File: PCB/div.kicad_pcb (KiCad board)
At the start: 2 copper layers, 31.5 x 110.5 mm, 74 parts, among them J1 Rst, J10 OUT, J2 Bus Gate Reset, J3 Clk, J4 PWR, J5 OUT, J6 OUT, J7 OUT, J8 OUT, J9 OUT, Q1 BC547, Q10 BC547, Q2 BC547, Q3 BC547, Q4 BC557, Q5 BC547, Q6 BC547, Q7 BC547, Q8 BC547, Q9 BC547, U1 4024

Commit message: :pencil2: Fix relevant DRC warnings
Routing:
- net Net-(D1-K): track 17.3 -> 16.7 mm
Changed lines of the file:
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@@
   (segment (start 143.383 50.165) (end 145.161 51.943) (width 0.2032) (layer "F.Cu") (net 4))
   (segment (start 144.1578 59.6772) (end 138.7982 59.6772) (width 0.2032) (layer "B.Cu") (net 4))
-  (segment (start 138.303 59.182) (end 138.684 58.801) (width 0.2032) (layer "B.Cu") (net 4))
   (segment (start 138.7982 59.6772) (end 138.303 59.182) (width 0.2032) (layer "B.Cu") (net 4))
   (segment (start 145.161 58.674) (end 144.1578 59.6772) (width 0.2032) (layer "B.Cu") (net 4))

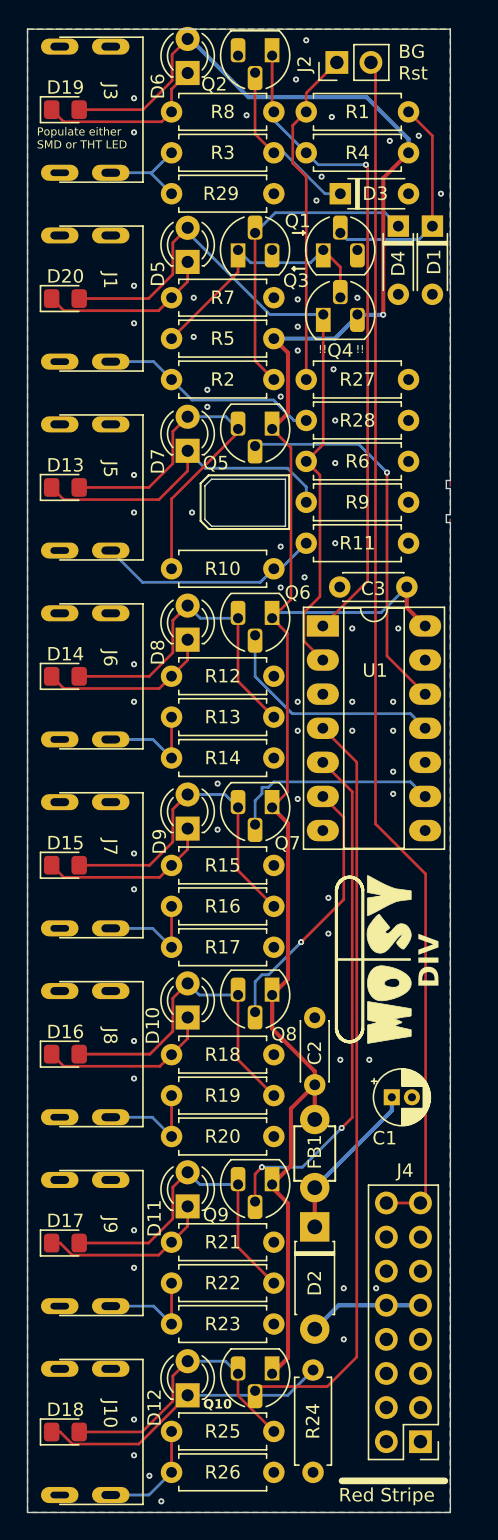
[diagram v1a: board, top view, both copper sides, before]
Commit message: :adhesive_bandaid: Fix DRC errors
Display of errors was accidentally switched off und with the change
of transistor footprints trace overlaps have been introduced.

These errors are now fixed.
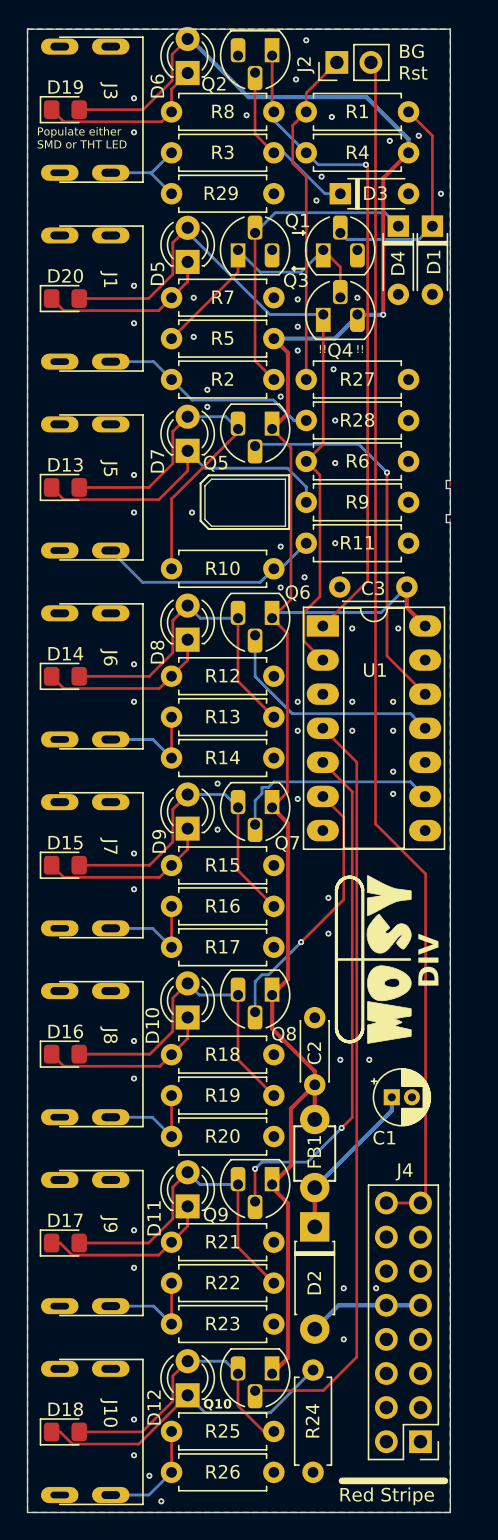
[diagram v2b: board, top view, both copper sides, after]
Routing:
- net Net-(D12-K): track 22.1 -> 23.2 mm
- net Net-(Q1-C): track 19.9 -> 20.4 mm
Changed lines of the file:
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@@
   (segment (start 117.434078 148.5) (end 118.337278 149.4032) (width 0.2032) (layer "F.Cu") (net 19))
   (segment (start 116.8 148.5) (end 117.434078 148.5) (width 0.2032) (layer "F.Cu") (net 19))
-  (segment (start 126.9282 145.77) (end 134.392 145.77) (width 0.2032) (layer "B.Cu") (net 19))
-  (segment (start 134.392 145.77) (end 136.271 143.891) (width 0.2032) (layer "B.Cu") (net 19))
+  (segment (start 126.9282 145.77) (end 128.2242 147.066) (width 0.2032) (layer "B.Cu") (net 19))
+  (segment (start 128.2242 147.066) (end 133.096 147.066) (width 0.2032) (layer "B.Cu") (net 19))
+  (segment (start 133.096 147.066) (end 136.271 143.891) (width 0.2032) (layer "B.Cu") (net 19))
   (segment (start 126.9282 143.23) (end 125.825 144.3332) (width 0.2032) (layer "F.Cu") (net 20))
+  (segment (start 130.683 146.558) (end 132.588 148.463) (width 0.2032) (layer "F.Cu") (net 20))
   (segment (start 123.534 148.5) (end 118.85 148.5) (width 0.2032) (layer "F.Cu") (net 20))
+  (segment (start 132.588 148.463) (end 133.35 148.463) (width 0.2032) (layer "F.Cu") (net 20))
   (segment (start 125.825 144.3332) (end 125.825 146.209) (width 0.2032) (layer "F.Cu") (net 20))
-  (segment (start 130.683 144.166) (end 130.683 145.796) (width 0.2032) (layer "F.Cu") (net 20))
-  (segment (start 130.683 145.796) (end 133.35 148.463) (width 0.2032) (layer "F.Cu") (net 20))
   (segment (start 125.825 146.209) (end 123.534 148.5) (width 0.2032) (layer "F.Cu") (net 20))
+  (segment (start 130.683 144.166) (end 130.683 146.558) (width 0.2032) (layer "F.Cu") (net 20))
   (segment (start 126.9282 143.23) (end 129.747 143.23) (width 0.2032) (layer "B.Cu") (net 20))
   (segment (start 129.747 143.23) (end 130.683 144.166) (width 0.2032) (layer "B.Cu") (net 20))
@@
   (segment (start 130.683 60.452) (end 130.683 62.103) (width 0.2032) (layer "F.Cu") (net 37))
   (segment (start 137.033 60.452) (end 138.303 61.722) (width 0.2032) (layer "F.Cu") (net 37))
-  (segment (start 131.6362 61.4052) (end 130.683 60.452) (width 0.2032) (layer "B.Cu") (net 37))
-  (segment (start 137.033 60.452) (end 136.0798 61.4052) (width 0.2032) (layer "B.Cu") (net 37))
-  (segment (start 136.0798 61.4052) (end 131.6362 61.4052) (width 0.2032) (layer "B.Cu") (net 37))
+  (segment (start 132.334 62.103) (end 130.683 60.452) (width 0.2032) (layer "B.Cu") (net 37))
+  (segment (start 137.033 60.452) (end 135.382 62.103) (width 0.2032) (layer "B.Cu") (net 37))
+  (segment (start 135.382 62.103) (end 132.334 62.103) (width 0.2032) (layer "B.Cu") (net 37))
   (segment (start 140.335 85.125) (end 137 88.46) (width 0.2032) (layer "F.Cu") (net 38))
   (segment (start 133.223 45.974) (end 133.223 50.038) (width 0.2032) (layer "F.Cu") (net 38))
@@
   (segment (start 135.382 112.014) (end 135.382 112.0188) (width 0.2032) (layer "B.Cu") (net 42))
   (segment (start 132.953 114.4478) (end 132.4698 114.4478) (width 0.2032) (layer "B.Cu") (net 42))
-  (segment (start 131.953 131.339) (end 131.953 129.286) (width 0.2032) (layer "F.Cu") (net 43))
-  (segment (start 131.953 129.286) (end 132.461 128.778) (width 0.2032) (layer "F.Cu") (net 43))
   (segment (start 138.4032 125.857) (end 139.192 125.0682) (width 0.2032) (layer "F.Cu") (net 43))
   (segment (start 139.192 100.812) (end 137 98.62) (width 0.2032) (layer "F.Cu") (net 43))
+  (segment (start 131.953 128.905) (end 131.953 131.339) (width 0.2032) (layer "F.Cu") (net 43))
   (segment (start 139.192 125.0682) (end 139.192 100.812) (width 0.2032) (layer "F.Cu") (net 43))
   (via (at 138.4032 125.857) (size 0.45) (drill 0.2) (layers "F.Cu" "B.Cu") (net 43))
-  (via (at 132.461 128.778) (size 0.45) (drill 0.2) (layers "F.Cu" "B.Cu") (net 43))
-  (segment (start 135.4822 128.778) (end 138.4032 125.857) (width 0.2032) (layer "B.Cu") (net 43))
-  (segment (start 132.461 128.778) (end 135.4822 128.778) (width 0.2032) (layer "B.Cu") (net 43))
+  (via (at 131.953 128.905) (size 0.45) (drill 0.2) (layers "F.Cu" "B.Cu") (net 43))
+  (segment (start 132.461 128.397) (end 135.8632 128.397) (width 0.2032) (layer "B.Cu") (net 43))
+  (segment (start 135.8632 128.397) (end 138.4032 125.857) (width 0.2032) (layer "B.Cu") (net 43))
+  (segment (start 131.953 128.905) (end 132.461 128.397) (width 0.2032) (layer "B.Cu") (net 43))
+  (segment (start 131.974 145.415) (end 131.953 145.436) (width 0.2032) (layer "F.Cu") (net 44))
+  (segment (start 137 96.08) (end 139.5258 98.6058) (width 0.2032) (layer "F.Cu") (net 44))
+  (segment (start 139.5258 142.9222) (end 137.033 145.415) (width 0.2032) (layer "F.Cu") (net 44))
+  (segment (start 137.033 145.415) (end 131.974 145.415) (width 0.2032) (layer "F.Cu") (net 44))
   (segment (start 139.5258 98.6058) (end 139.5258 142.9222) (width 0.2032) (layer "F.Cu") (net 44))
-  (segment (start 137.3288 145.1192) (end 132.2698 145.1192) (width 0.2032) (layer "F.Cu") (net 44))
-  (segment (start 139.5258 142.9222) (end 137.3288 145.1192) (width 0.2032) (layer "F.Cu") (net 44))
-  (segment (start 137 96.08) (end 139.5258 98.6058) (width 0.2032) (layer "F.Cu") (net 44))
-  (segment (start 132.2698 145.1192) (end 131.953 145.436) (width 0.2032) (layer "F.Cu") (net 44))
   (segment (start 126.9282 62.8098) (end 126.9282 61.341) (width 0.2032) (layer "F.Cu") (net 52))
   (segment (start 116.8 64.0714) (end 117.7032 64.9746) (width 0.2032) (layer "F.Cu") (net 52))

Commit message: :lipstick: Perform a Geographical Reannotation on the PCB
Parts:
- renumbered C3 to C1, C1 to C3, D6 to D1, D8 to D10, D14 to D11, D9 to D12, D15 to D13, D10 to D14, D16 to D15, D11 to D16, D2 to D17, D17 to D18, D12 to D19, D19 to D2, D18 to D20, D1 to D5, D5 to D6, D20 to D7, D7 to D8, D13 to D9, J2 to J1, J4 to J10, J3 to J2, J1 to J3, J5 to J4, J6 to J5, J7 to J6, J8 to J7, J9 to J8, J10 to J9, Q2 to Q1, Q3 to Q2, Q1 to Q3, R8 to R1, R28 to R10, R6 to R11, R9 to R12, R11 to R13, R10 to R14, R12 to R15, R13 to R16, R14 to R17, R15 to R18, R16 to R19, R1 to R2, R17 to R20, R18 to R21, R19 to R22, R20 to R23, R21 to R24, R22 to R25, R23 to R26, R25 to R27, R26 to R28, R24 to R29, R29 to R5, R7 to R6, R5 to R7, R2 to R8, R27 to R9
